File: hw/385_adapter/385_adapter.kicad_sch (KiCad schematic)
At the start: 4 parts, among them J1 Conn_02x18_Odd_Even, J2 Conn_01x03, J3 Conn_02x01

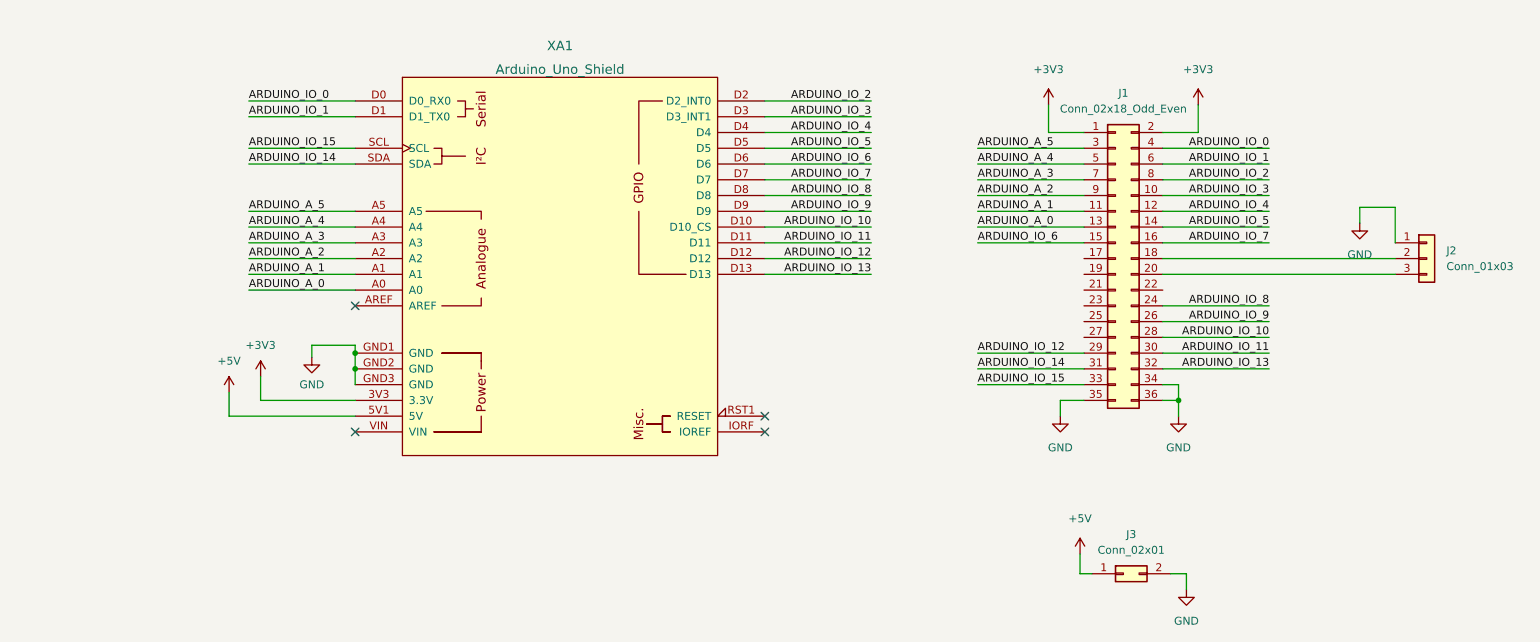
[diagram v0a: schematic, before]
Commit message: Add text labels to arduino pins
I finally found the schematics for the 385 board so now there can be
labels for what the pins actually do.
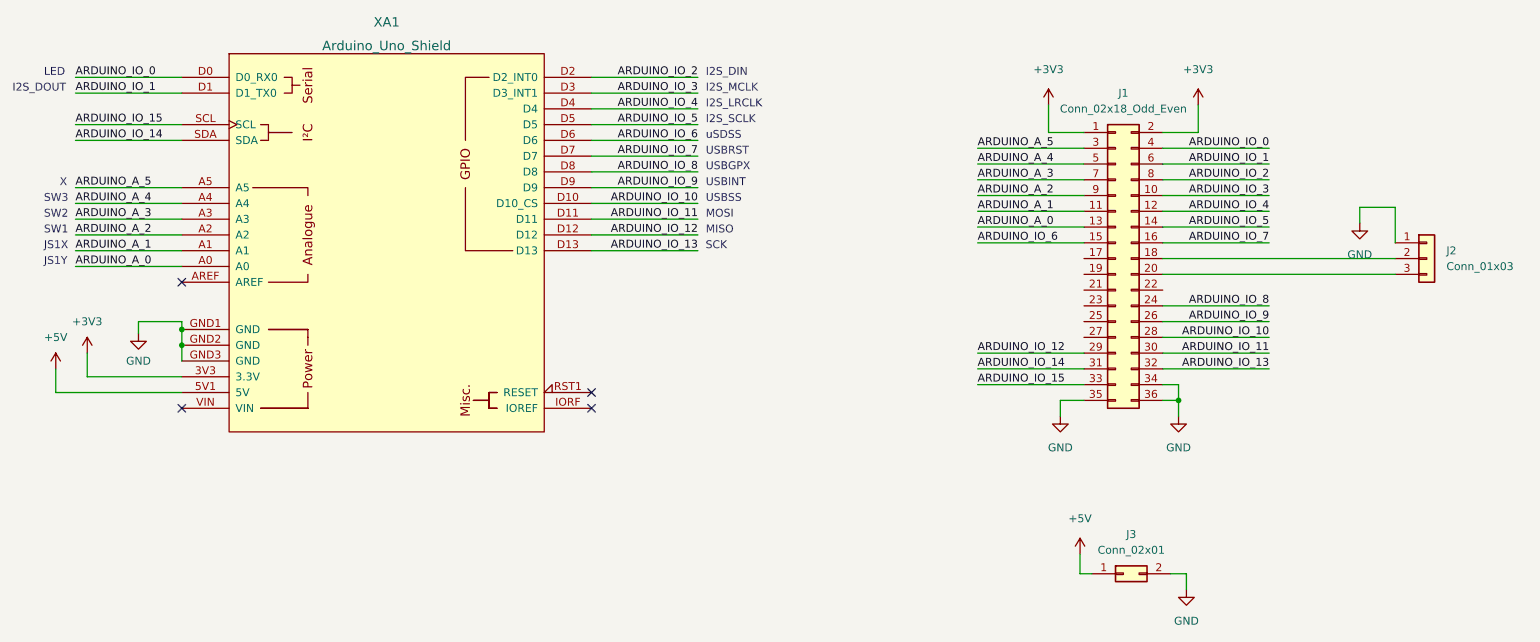
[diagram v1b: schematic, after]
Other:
- note added: "I2S_DIN"
- note added: "I2S_DOUT"
- note added: "I2S_LRCLK"
- note added: "I2S_MCLK"
- note added: "I2S_SCLK"
- note added: "JS1X"
- note added: "JS1Y"
- note added: "LED"
- note added: "MISO"
- note added: "MOSI"
- note added: "SCK"
- note added: "SW1"
- note added: "SW2"
- note added: "SW3"
- note added: "USBGPX"
- note added: "USBINT"
- note added: "USBRST"
- note added: "USBSS"
- note added: "X"
- note added: "uSDSS"
- moved on the sheet: XA1

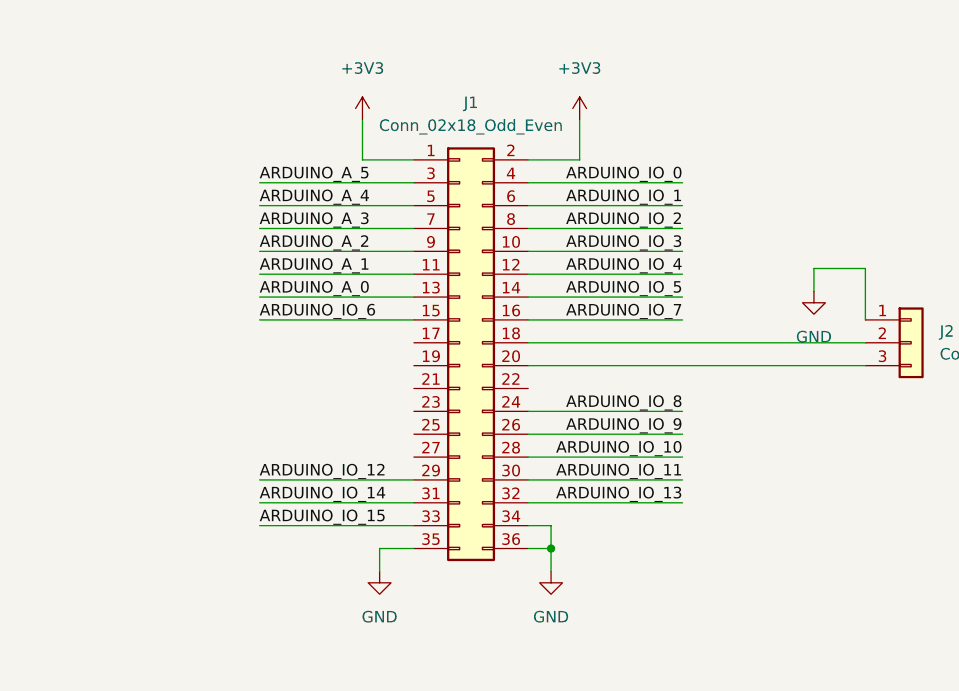
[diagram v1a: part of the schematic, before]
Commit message: Add labels on fpga side
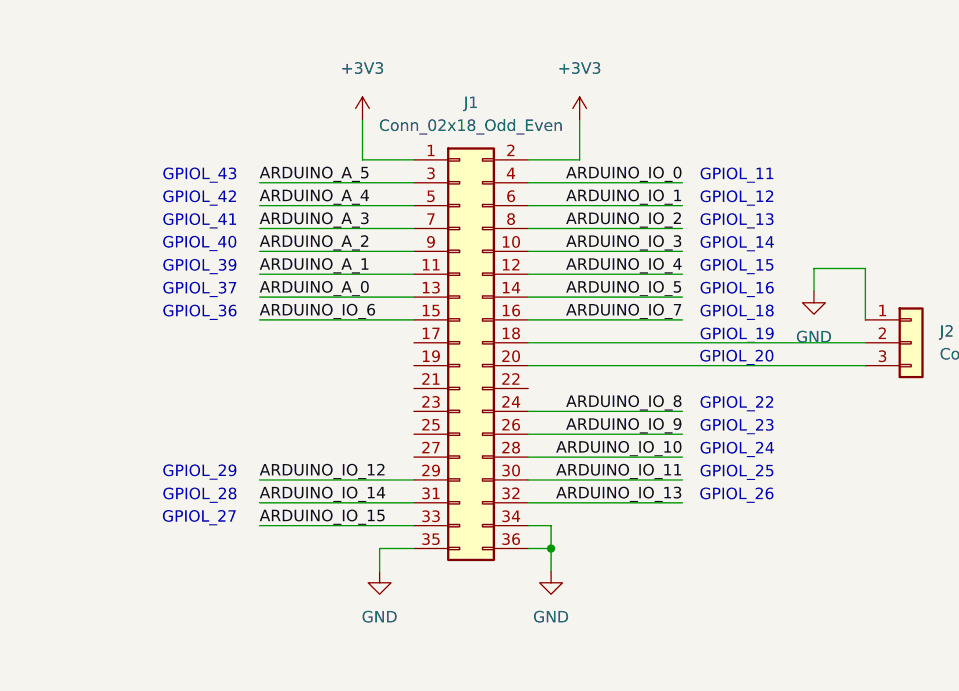
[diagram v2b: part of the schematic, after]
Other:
- note added: "GPIOL_11"
- note added: "GPIOL_12"
- note added: "GPIOL_13"
- note added: "GPIOL_14"
- note added: "GPIOL_15"
- note added: "GPIOL_16"
- note added: "GPIOL_18"
- note added: "GPIOL_19"
- note added: "GPIOL_20"
- note added: "GPIOL_22"
- note added: "GPIOL_23"
- note added: "GPIOL_24"
- note added: "GPIOL_25"
- note added: "GPIOL_26"
- note added: "GPIOL_27"
- note added: "GPIOL_28"
- note added: "GPIOL_29"
- note added: "GPIOL_36"
- note added: "GPIOL_37"
- note added: "GPIOL_39"
- note added: "GPIOL_40"
- note added: "GPIOL_41"
- note added: "GPIOL_42"
- note added: "GPIOL_43"
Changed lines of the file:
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@@
     (stroke (width 0) (type default) (color 0 0 0 0))
   )
+  (text "GPIOL_28" (at 175.26 102.87 0)
+    (effects (font (size 1.27 1.27)) (justify left bottom))
+  )
+  (text "GPIOL_16" (at 234.95 80.01 0)
+    (effects (font (size 1.27 1.27)) (justify left bottom))
+  )
   (text "JS1Y" (at 35.56 86.36 0)
+    (effects (font (size 1.27 1.27)) (justify left bottom))
+  )
+  (text "GPIOL_14" (at 234.95 74.93 0)
+    (effects (font (size 1.27 1.27)) (justify left bottom))
+  )
+  (text "GPIOL_39" (at 175.26 77.47 0)
+    (effects (font (size 1.27 1.27)) (justify left bottom))
+  )
+  (text "GPIOL_40" (at 175.2392 74.9031 0)
+    (effects (font (size 1.27 1.27)) (justify left bottom))
+  )
+  (text "GPIOL_36" (at 175.26 82.55 0)
     (effects (font (size 1.27 1.27)) (justify left bottom))
   )
@@
     (effects (font (size 1.27 1.27)) (justify left bottom))
   )
+  (text "GPIOL_11" (at 234.95 67.31 0)
+    (effects (font (size 1.27 1.27)) (justify left bottom))
+  )
+  (text "GPIOL_41" (at 175.26 72.39 0)
+    (effects (font (size 1.27 1.27)) (justify left bottom))
+  )
+  (text "GPIOL_20" (at 234.9176 87.5645 0)
+    (effects (font (size 1.27 1.27)) (justify left bottom))
+  )
   (text "SW1" (at 35.56 81.28 0)
     (effects (font (size 1.27 1.27)) (justify left bottom))
   )
   (text "X" (at 38.1 73.66 0)
+    (effects (font (size 1.27 1.27)) (justify left bottom))
+  )
+  (text "GPIOL_27" (at 175.2097 105.3696 0)
     (effects (font (size 1.27 1.27)) (justify left bottom))
   )
@@
     (effects (font (size 1.27 1.27)) (justify left bottom))
   )
+  (text "GPIOL_24" (at 234.95 97.79 0)
+    (effects (font (size 1.27 1.27)) (justify left bottom))
+  )
   (text "SCK" (at 142.2082 83.8199 0)
     (effects (font (size 1.27 1.27)) (justify left bottom))
@@
     (effects (font (size 1.27 1.27)) (justify left bottom))
   )
+  (text "GPIOL_25" (at 234.95 100.33 0)
+    (effects (font (size 1.27 1.27)) (justify left bottom))
+  )
+  (text "GPIOL_43" (at 175.26 67.31 0)
+    (effects (font (size 1.27 1.27)) (justify left bottom))
+  )
+  (text "GPIOL_19" (at 234.95 85.09 0)
+    (effects (font (size 1.27 1.27)) (justify left bottom))
+  )
+  (text "GPIOL_42" (at 175.26 69.85 0)
+    (effects (font (size 1.27 1.27)) (justify left bottom))
+  )
   (text "uSDSS" (at 142.24 66.04 0)
+    (effects (font (size 1.27 1.27)) (justify left bottom))
+  )
+  (text "GPIOL_15" (at 234.95 77.47 0)
     (effects (font (size 1.27 1.27)) (justify left bottom))
   )
@@
   )
   (text "MOSI" (at 142.24 78.74 0)
+    (effects (font (size 1.27 1.27)) (justify left bottom))
+  )
+  (text "GPIOL_18" (at 234.95 82.55 0)
     (effects (font (size 1.27 1.27)) (justify left bottom))
   )
@@
     (effects (font (size 1.27 1.27)) (justify left bottom))
   )
+  (text "GPIOL_29" (at 175.2563 100.2994 0)
+    (effects (font (size 1.27 1.27)) (justify left bottom))
+  )
+  (text "GPIOL_12" (at 234.95 69.85 0)
+    (effects (font (size 1.27 1.27)) (justify left bottom))
+  )
+  (text "GPIOL_22" (at 234.95 92.71 0)
+    (effects (font (size 1.27 1.27)) (justify left bottom))
+  )
   (text "I2S_DIN" (at 142.24 55.88 0)
+    (effects (font (size 1.27 1.27)) (justify left bottom))
+  )
+  (text "GPIOL_37" (at 175.26 80.01 0)
+    (effects (font (size 1.27 1.27)) (justify left bottom))
+  )
+  (text "GPIOL_13" (at 234.95 72.39 0)
     (effects (font (size 1.27 1.27)) (justify left bottom))
   )
@@
     (effects (font (size 1.27 1.27)) (justify left bottom))
   )
+  (text "GPIOL_23" (at 234.95 95.25 0)
+    (effects (font (size 1.27 1.27)) (justify left bottom))
+  )
+  (text "GPIOL_26" (at 234.9176 102.8669 0)
+    (effects (font (size 1.27 1.27)) (justify left bottom))
+  )

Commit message: Add labels for sd mode
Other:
- note added: "MISO (sd_data)"
- note added: "MOSI (sd_cmd)"
- note added: "SCK (sd_clk)"
- note removed: "MISO"
- note removed: "MOSI"
- note removed: "SCK"
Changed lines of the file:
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@@
     (effects (font (size 1.27 1.27)) (justify left bottom))
   )
-  (text "MISO" (at 142.24 81.28 0)
+  (text "MISO (sd_data)" (at 142.24 81.28 0)
     (effects (font (size 1.27 1.27)) (justify left bottom))
   )
@@
     (effects (font (size 1.27 1.27)) (justify left bottom))
   )
-  (text "SCK" (at 142.2082 83.8199 0)
+  (text "SCK (sd_clk)" (at 142.2082 83.8199 0)
     (effects (font (size 1.27 1.27)) (justify left bottom))
   )
@@
     (effects (font (size 1.27 1.27)) (justify left bottom))
   )
-  (text "MOSI" (at 142.24 78.74 0)
+  (text "MOSI (sd_cmd)" (at 142.24 78.74 0)
     (effects (font (size 1.27 1.27)) (justify left bottom))
   )
